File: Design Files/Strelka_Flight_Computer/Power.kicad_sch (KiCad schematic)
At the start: 60 parts, among them J1 1S_LiPo_LARGE_HOLE_XT-30, Q1 ??, Q2 ??, SW3 SW_DIP_x01, U1 FP6276BXR-G1, U16 TPS61085DGKR, U2 AP9101CK6, U3 AMS1117-3.3

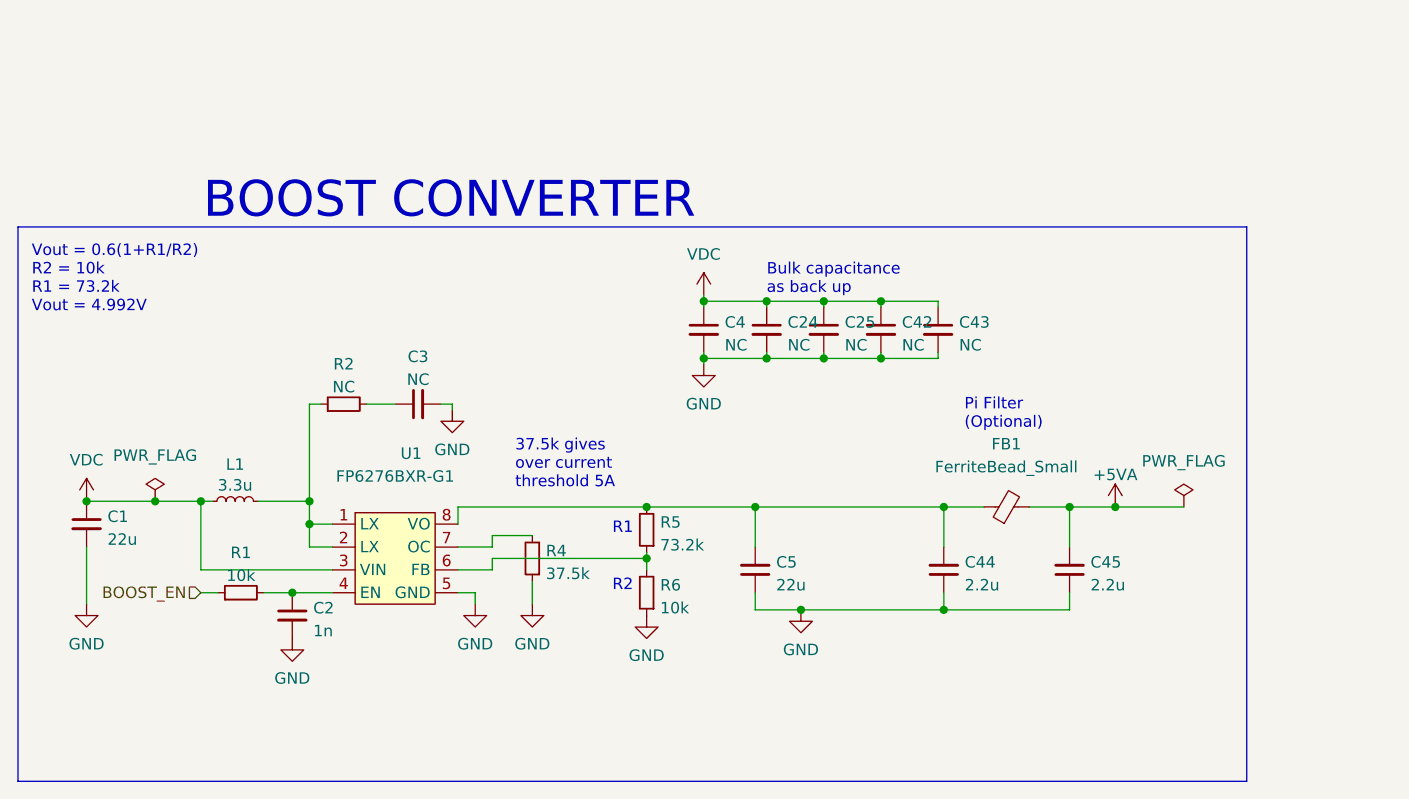
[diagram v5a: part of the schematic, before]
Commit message: Deleted extra boost circuit and L80 schematic
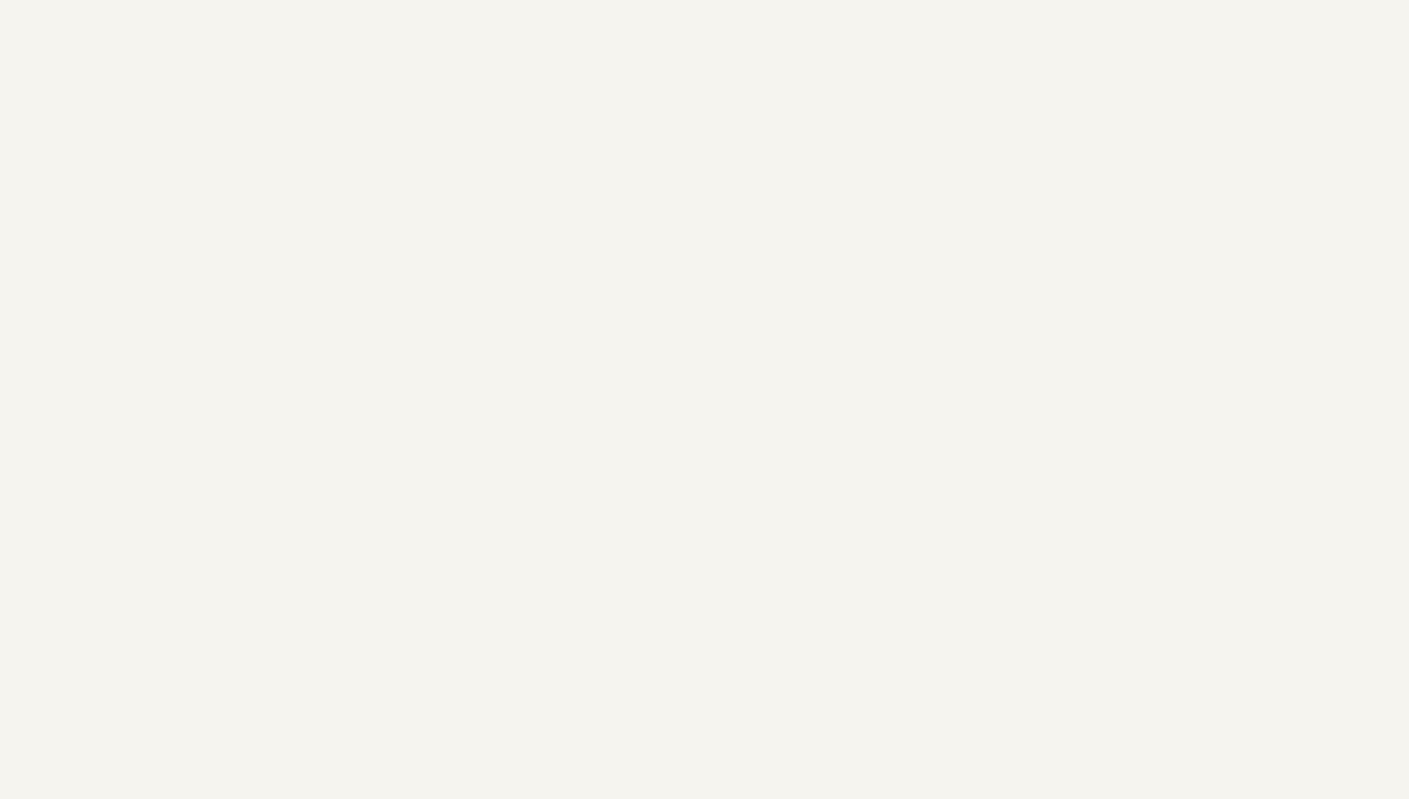
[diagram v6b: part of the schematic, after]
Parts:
- removed C1, C5: 22u, Capacitor_SMD:C_0603_1608Metric, symbol Device:C_Small
- removed C2: 1n, Capacitor_SMD:C_0603_1608Metric, symbol Device:C_Small
- removed C24, C25, C3, C4, C42, C43: NC, Capacitor_SMD:C_0603_1608Metric, symbol Device:C_Small
- removed C44, C45: 2.2u, Capacitor_SMD:C_0603_1608Metric, symbol Device:C_Small
- removed FB1: FerriteBead_Small, Inductor_SMD:L_0603_1608Metric, symbol Device:FerriteBead_Small
- removed L1: 3.3u, Inductor_SMD:L_Vishay_IHLP-2020, symbol Device:L_Small
- removed R1, R6: 10k, Resistor_SMD:R_0603_1608Metric, symbol Device:R_Small
- removed R2: NC, Resistor_SMD:R_0603_1608Metric, symbol Device:R_Small
- removed R4: 37.5k, Resistor_SMD:R_0603_1608Metric, symbol Device:R_Small
- removed R5: 73.2k, Resistor_SMD:R_0603_1608Metric, symbol Device:R_Small
- removed U1: FP6276BXR-G1, Package_SO:Diodes_PSOP-8, symbol FP6276BXR-G1:FP6276BXR-G1
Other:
- note removed: "37.5k gives over current threshold 5A"
- note removed: "Pi Filter (Optional)"
- note removed: "R1"
- note removed: "R2"
- note removed: "Vout = 0.6(1+R1/R2) R2 = 10k R1 = 73.2k Vout = 4.992V"

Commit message: Started component placement
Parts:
- L2: footprint https:__datasheet.lcsc.com_lcsc_2105092345_BOURNS-SRP5030T-6R8M_C1329837.pdf -> Inductor_SMD:L_Bourns_SRP5030T
- MOSFET1: footprint footprints:DMG6968UDM-7 -> Footprints:DMG6968UDM-7
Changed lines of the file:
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@@
       (effects (font (size 1.524 1.524)))
     )
-    (property "Footprint" "footprints:DMG6968UDM-7" (id 2) (at 146.05 63.754 0)
+    (property "Footprint" "Footprints:DMG6968UDM-7" (id 2) (at 146.05 63.754 0)
       (effects (font (size 1.524 1.524)) hide)
     )
@@
     (property "Reference" "L2" (id 0) (at 91.44 128.905 90))
     (property "Value" "6u" (id 1) (at 91.44 130.81 90))
-    (property "Footprint" "https:__datasheet.lcsc.com_lcsc_2105092345_BOURNS-SRP5030T-6R8M_C1329837.pdf" (id 2) (at 91.44 132.715 0)
-      (effects (font (size 1.27 1.27)) hide)
-    )
+    (property "Footprint" "Inductor_SMD:L_Bourns_SRP5030T" (id 2) (at 91.44 132.715 0)
+      (effects (font (size 1.27 1.27)) hide)
+    )

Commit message: Creating BOM
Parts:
- C55: value 68u -> 47u
- C56: value NC -> 47u; footprint Capacitor_SMD:C_0603_1608Metric -> Capacitor_SMD:C_0805_2012Metric
- C57: footprint Capacitor_SMD:C_0603_1608Metric -> Capacitor_SMD:C_0805_2012Metric
- D1, D2, D4: LCSC# (none) -> C8598
- MOSFET1: LCSC# (none) -> C151635; MFR# DMG6968UDM-7 -> (none)
- Q1, Q2: value ?? -> CJK2333; LCSC# (none) -> C504109
- SW3: value SW_DIP_x01 -> SM02B-GHS-TB(LF)(SN); LCSC# (none) -> C189893
- U16: AVAILABILITY Unavailable -> (none); DESCRIPTION 18.5V, 2A, 650kHz / 1.2MHz Step-Up DC-DC Converter w/ Force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 -> (none); LCSC# (none) -> C113659; MF Texas Instruments -> (none); MOUSER-PURCHASE-URL https://snapeda.com/shop?store=Mouser&id=1236975 -> (none); MP TPS61085DGKR -> (none); PACKAGE VSSOP-8 Texas Instruments -> (none); PRICE None -> (none); TEXAS_INSTRUMENTS-PURCHASE-URL https://snapeda.com/shop?store=Texas+Instruments&id=1236975 -> (none)
- U2: LCSC# (none) -> C151339
- U3: LCSC# (none) -> C173386
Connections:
- net GND: no longer U16.4 (PGND)
- net VDC: no longer U16.7 (FREQ)
- net at R62.1, R63.2: no longer U16.2 (FB)
- net at R61.2: no longer U16.1 (COMP)
- net at D14.2 (A), L2.2: no longer U16.5 (SW)
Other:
- moved on the sheet: C41, C46, C47, C48, C50, C51, C52, C53, C54, C55, C56, C57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
